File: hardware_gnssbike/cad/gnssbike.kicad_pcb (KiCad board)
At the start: 4 copper layers, 34 x 90 mm, 128 parts, among them J101 Molex 2036150003, J102 JST SM06B-GHS-TB, J103 contato de mola, 2 vias, J104 contato de mola, 2 vias, J105 contato de mola, 2 vias, J201 Tag-Connect TC2030-NL, J302 contato de mola, 2 vias, J401 Hirose FH28-10S-0.5SH, J402 Molex 503480-0500, Q401 DMG1012T-7, Q601 DMG1012T-7, Q602 DMG1012T-7, Q603 DMG1012T-7, SW601 Omron B3S-1002P, SW602 Omron B3S-1002P, SW603 Omron B3S-1002P, U101 nPM1300-QEAA, U102 MAX17262REWL, U103 AEM10900, U104 TPS7A0218PDQN, U201 MinewSemi ME54BS13, U301 u-blox MAX-F10S, U302 TI TXU0204BQAR, U501 MX25R6435F, U502 Bosch BMP585, U503 Bosch BMI270, U504 MMC5633NJL, U505 TI OPT3001DNPR

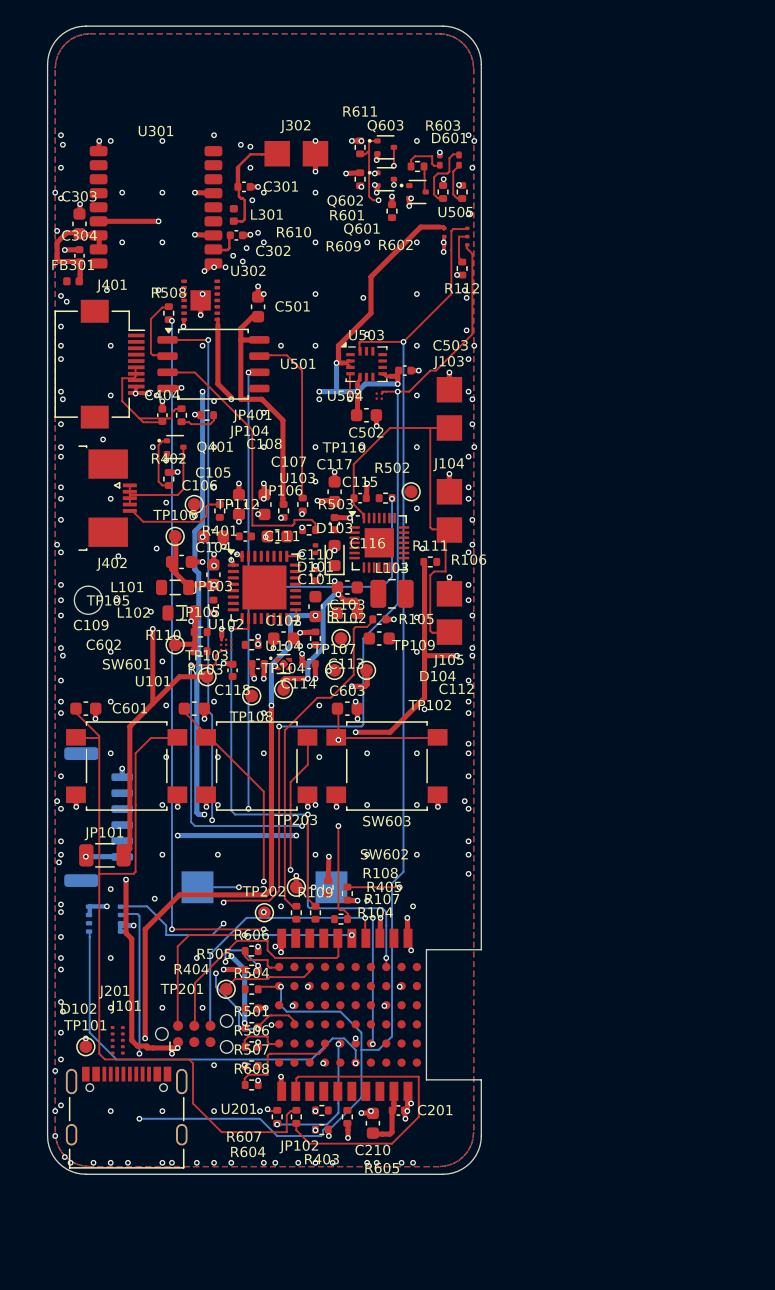
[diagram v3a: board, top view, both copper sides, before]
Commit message: feat(hardware): draw each part as its own symbol, not as a block
A rectangle with pin names down its sides is how an INTEGRATED CIRCUIT is
drawn, and only an integrated circuit. This generator drew all 127 parts
that way - resistors, ceramic capacitors, diodes, the TVS - and a sheet of
blocks joined by lines does not show a circuit.

Every class has its own symbol now, in the standard form, with the lead
axis on x and the body between -1.27 and +1.27 mm: a zigzag for a resistor
and a 0 ohm link (42 of them), two parallel plates for a ceramic capacitor
and a curved plate with a + for an electrolytic (31), four arcs for an
inductor (4), the same arcs inside a rectangle for a ferrite bead, which is
what tells the two apart, a zigzag with a diagonal arrow for the thermistor,
a triangle and a bar for a diode with arrows leaving it for an LED, two
contacts with a bar and a plunger for a key, a circle with a diagonal for
the buzzer, and a circle on the end of a lead for a test point. The 36 that
stay rectangles are the ones that should be: the ICs, the connectors and the
display. A two terminal part no longer prints pin numbers or pin names -
"1" and "2" on a resistor is noise, and the symbol already says which end is
which where it matters.

The power symbols had room reserved for the symbol and none for its NAME:
two ground pins two grid steps apart each got their own symbol, the symbols
did not collide, and the words printed over each other - "GNDGNDGND" along
the bottom of every chip. What is reserved now is the whole thing. With a
limit: the first cut let the stub run to fourteen grid steps looking for a
clear spot, and one of them crossed a component and split a net. A long stub
is worse than a crowded label, so it stops at eight and the label gives way.

One attempt is NOT in this commit, on purpose. Grouping every pin of a rail
on one edge into a single symbol - which is what a person draws - joins the
stubs with a line that runs along the part's edge and crosses w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
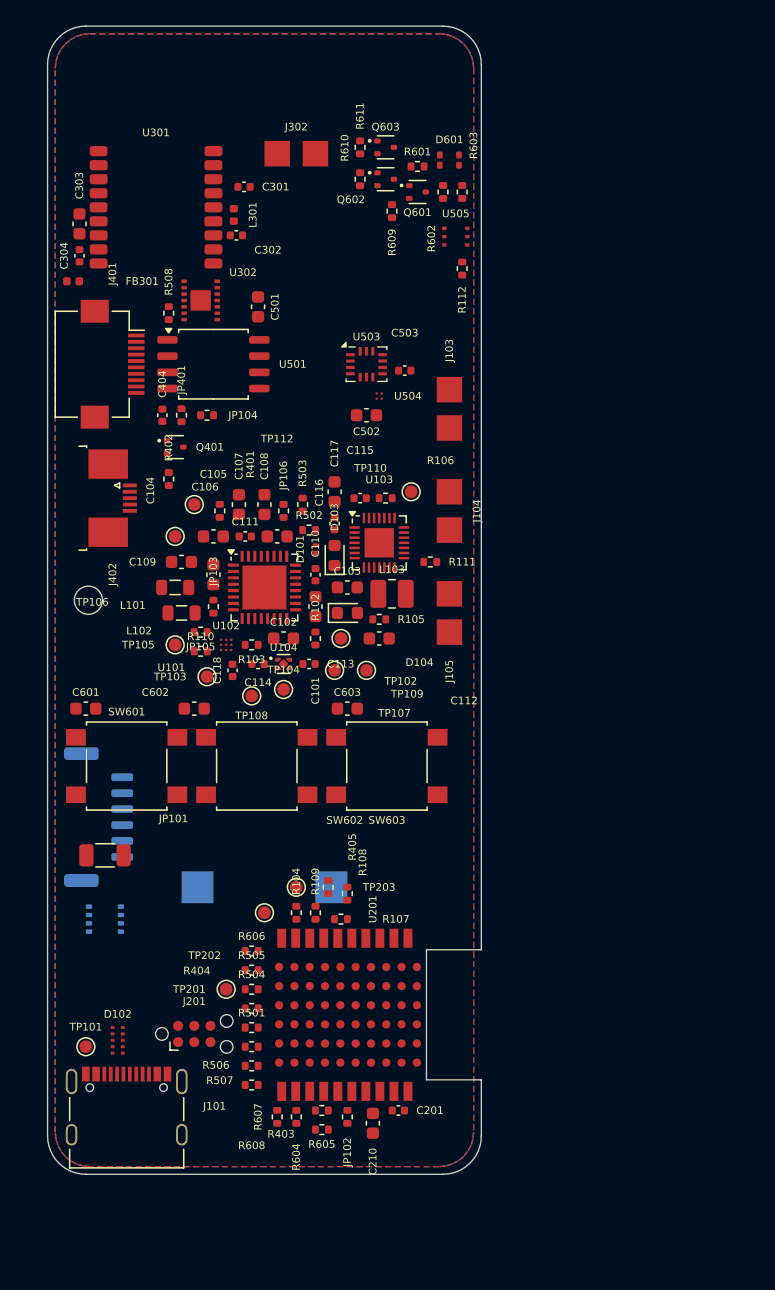
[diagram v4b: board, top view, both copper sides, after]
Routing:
- net 3V0: track 201.5 -> 0.00 mm, vias 18 -> 0
- net SENS_SDA: track 125.8 -> 0.00 mm, vias 4 -> 0
- net 3V0_SENS: track 108.0 -> 0.00 mm, vias 9 -> 0
- net SENS_SCL: track 86.6 -> 0.00 mm, vias 6 -> 0
- net RGB_B: track 74.7 -> 0.00 mm, vias 2 -> 0
- net KEY_L_SW: track 66.9 -> 0.00 mm
- net VBCKP: track 65.4 -> 0.00 mm, vias 3 -> 0
- net NOR_CS: track 63.5 -> 0.00 mm, vias 4 -> 0
- net NOR_MISO: track 63.1 -> 0.00 mm, vias 4 -> 0
- net GND: track 62.1 -> 0.00 mm, vias 285 -> 0
- net VSYS: track 55.8 -> 0.00 mm, vias 5 -> 0
- net KEY_C_SW: track 54.7 -> 0.00 mm, vias 3 -> 0
- net NOR_SCK_F: track 54.0 -> 0.00 mm, vias 3 -> 0
- net IMU_INT: track 53.4 -> 0.00 mm, vias 3 -> 0
- net SD3V0: track 53.4 -> 0.00 mm, vias 6 -> 0
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
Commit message: feat(hardware): a u.FL for the GNSS antenna, and an assembly drawing that reads
The GNSS antenna arrived on a spring contact. The line it feeds is the
L1 + L5 path of the MAX-F10S and section 4.4 of the integration manual asks
for 50 ohm on ALL of it - and a pair of gold pads that a leaf spring presses
on has no defined impedance at 1.2 and 1.6 GHz, no defined return path, and
a contact resistance that changes with how the case was closed. J302 is a
Hirose U.FL-R-SMT-1 now, the 50 ohm coaxial transition every GNSS module
reference design uses for an external element. It costs 2.6 x 2.6 mm of
board and trades a mechanical fit for a cable, which is a mechanical
decision that was recorded nowhere. The RF path went from 8.2 to 5.7 mm.
The three solar spring contacts stay spring contacts: no RF there.

And the assembly drawing stopped coming out of a KiCad layer, because
neither layer can give one for this board. Silkscreen is silkscreen: it
obeys manufacturing, 0.6 mm of text, and 127 designators on a 34 x 90 mm
board at 48% occupancy do not fit around the parts without landing on one
another or drifting so far from the part that they name nothing. F.Fab
carries whatever each library footprint put there, at whatever size its
author chose, plus the value - "TP110" at 1.0 mm beside "100 nF" at 0.5,
both over the outline.

An assembly drawing is not a copper layer. It is a drawing, and it may do
the one thing a silkscreen may not: put the label where it can be read and
draw a LINE from the label to the part. montagem.py does that - the
reference inside the courtyard where it fits, outside with a dot and a
leader where it does not. 92 of the 127 need the leader.

The silkscreen placement was also backwards: it preferred a spot clear of
ANY part's outline to a spot near its own, which on a board this dense
pushes the designator millimetres away and produces a cloud where nothing
points at anything. Proximity decides now - nearest first, the first
candidate that misses every 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
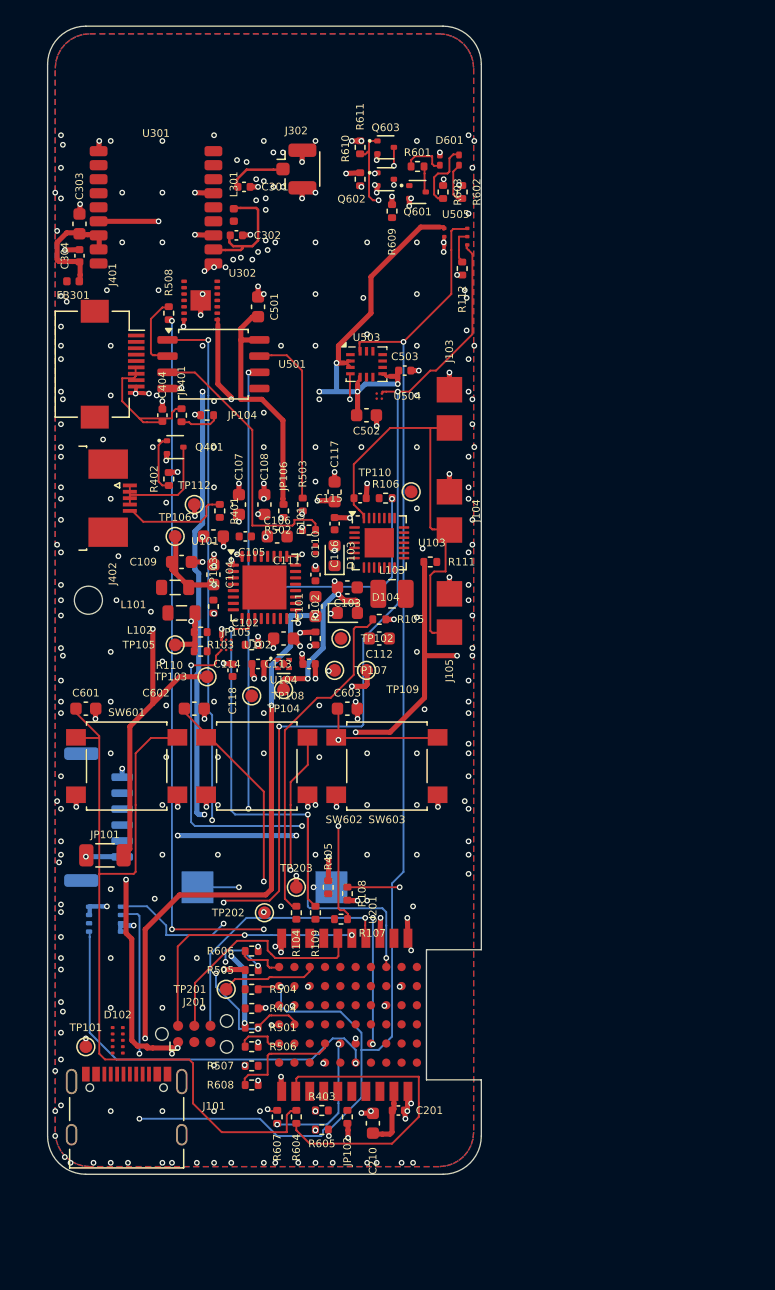
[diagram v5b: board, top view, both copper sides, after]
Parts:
- J302: value contato de mola, 2 vias -> Hirose U.FL-R-SMT-1; footprint gnssbike:ContatoMola_2x2mm_P3mm -> Connector_Coaxial:U.FL_Hirose_U.FL-R-SMT-1_Vertical
- moved J302 1.20 mm to (44.5, 36.2)
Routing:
- net 3V0: track 0.00 -> 201.5 mm, vias 0 -> 18
- net SENS_SDA: track 0.00 -> 125.8 mm, vias 0 -> 4
- net 3V0_SENS: track 0.00 -> 108.0 mm, vias 0 -> 9
- net SENS_SCL: track 0.00 -> 86.6 mm, vias 0 -> 6
- net RGB_B: track 0.00 -> 74.7 mm, vias 0 -> 2
- net KEY_L_SW: track 0.00 -> 66.9 mm
- net VBCKP: track 0.00 -> 65.4 mm, vias 0 -> 3
- net NOR_CS: track 0.00 -> 63.5 mm, vias 0 -> 4
- net NOR_MISO: track 0.00 -> 63.1 mm, vias 0 -> 4
- net GND: track 0.00 -> 62.5 mm, vias 0 -> 295
- net VSYS: track 0.00 -> 55.8 mm, vias 0 -> 5
- net KEY_C_SW: track 0.00 -> 54.7 mm, vias 0 -> 3
- net NOR_SCK_F: track 0.00 -> 54.0 mm, vias 0 -> 3
- net IMU_INT: track 0.00 -> 53.4 mm, vias 0 -> 3
- net SD3V0: track 0.00 -> 53.4 mm, vias 0 -> 6
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
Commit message: feat(hardware): buy what JLCPCB can actually assemble
The board is made and assembled at JLCPCB, so every part has to be one
LCSC stocks - the owner's rule of 2026-09-24, with the Minew module and
the solar cells as the only exceptions. Three surveys against LCSC's
catalogue and JLCPCB's assembly API checked the 34 parts that are not a
plain resistor or capacitor, and this is what came back.

Parts that changed, and what each change costs:

  J101  Molex 2036150003 -> HRO TYPE-C-31-M-12 (C165948). 309 in the
        world at US$ 5,69 against 91.943 at US$ 0,186, and KiCad carries
        the land pattern under the part's own name. The body goes from
        8,58 to 7,35 mm, so the case opening changes.
  D101  ESD761DPYR -> TPD1E05U06DPYR (C436349). Same X1SON-2 and better
        capacitance, but bidirectional 24 V becomes unidirectional
        5,5 V: orientation now matters and a faulty cable putting 20 V
        on a CC line is no longer survivable.
  J103  three pairs of spring pads -> one JST ZH of 4 ways, with three
        0 ohm joining the groups to SRC. Nobody assembles a spring, a
        bicycle vibrates, and a pressed contact that opens and closes on
        the input of a switching converter is a dirty transient. ZH of
        1,5 mm on purpose: the cell is a GH of 1,25 and 4,2 V into the
        harvester's 2,73 V input would kill it. The 0 ohm let one face
        be measured alone in the sun.
  D105  new: a clamp on SRC. The right connector stops the mistake; the
        clamp stops the damage when the mistake comes from a crimp.
  J101  the shell had no pin, so four pads of the land pattern floated.

U101 and U103 stay as they are and go by consignment: the nPM1300 QFN is
zero on both sides and the whole e-peas line is zero. The nPM1300 does
exist in WLCSP-35, but its 0,419 x 0,440 mm ball pitch is smaller than
this board's 0,45 mm via and would force via-in-pad on every board ever
made, probably six layers, twice the thermal resistance and a light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
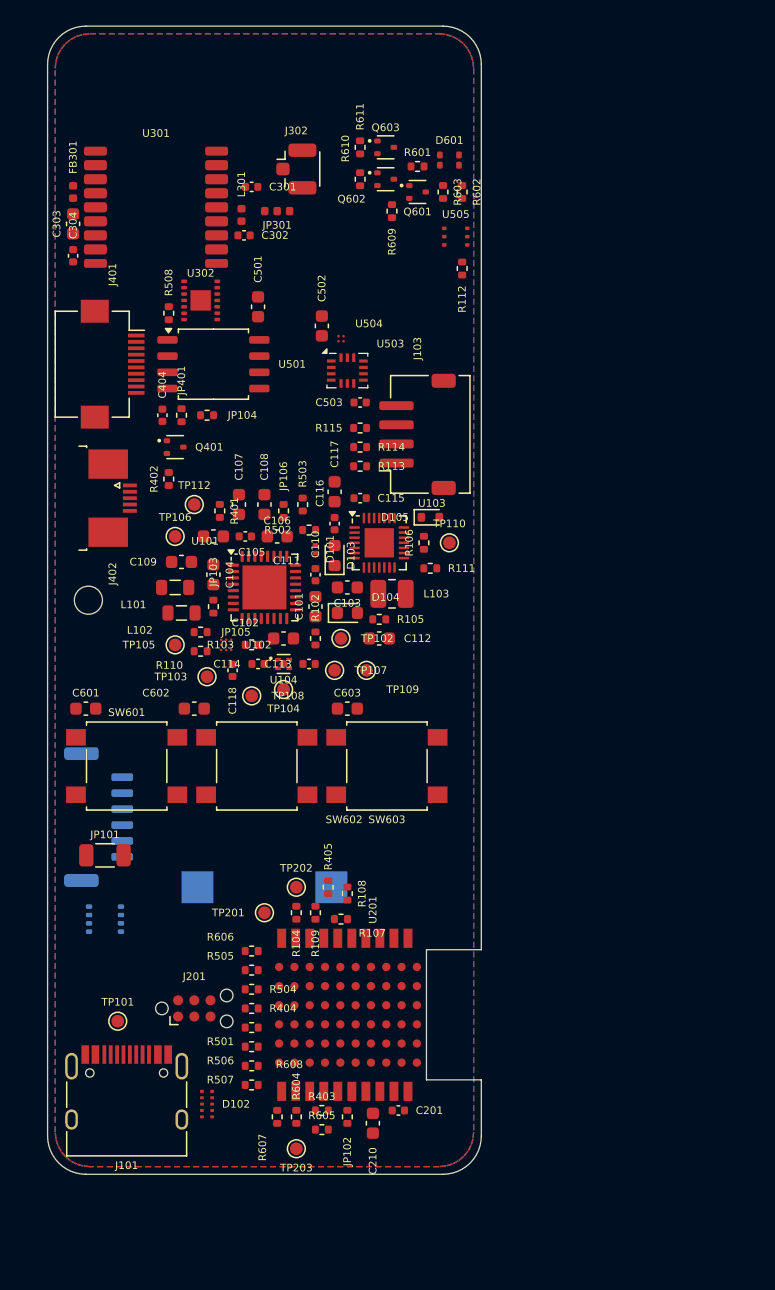
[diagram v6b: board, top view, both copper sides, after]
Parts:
- removed J104, J105: contato de mola, 2 vias, gnssbike:ContatoMola_2x2mm_P3mm
- added D105: TVS 3,0 V, Diode_SMD:D_SOD-523, F.Cu at (55.0, 63.5)
- added JP301: 0 R, gnssbike:JumperRF_3x0402, F.Cu at (43.0, 39.5)
- added R113: 0 R, Resistor_SMD:R_0402_1005Metric, F.Cu at (49.5, 59.5)
- added R114: 0 R, Resistor_SMD:R_0402_1005Metric, F.Cu at (49.5, 58.0)
- added R115: 0 R, Resistor_SMD:R_0402_1005Metric, F.Cu at (49.5, 56.5)
- D101: value ESD761DPYR -> TPD1E05U06DPYR
- J101: value Molex 2036150003 -> HRO TYPE-C-31-M-12; footprint Connector_USB:USB_C_Receptacle_Palconn_UTC16-G -> Connector_USB:USB_C_Receptacle_HRO_TYPE-C-31-M-12
- J103: value contato de mola, 2 vias -> JST S4B-ZR-SM4A-TF; footprint gnssbike:ContatoMola_2x2mm_P3mm -> Connector_JST:JST_ZH_S4B-ZR-SM4A-TF_1x04-1MP_P1.50mm_Horizontal
- U301: footprint gnssbike:u-blox_MAX-F10S_9.7x10.1mm -> gnssbike:u-blox_MAX_LCC-18_9.7x10.1mm
- U501: footprint Package_SO:SOIC-8_5.23x5.23mm_P1.27mm -> Package_SO:SOIC-8_5.275x5.275mm_P1.27mm
- moved TP203 20.5 mm to (44.5, 113.0)
- moved D102 8.60 mm to (37.5, 109.5)
- moved C502 7.83 mm to (46.5, 48.5), turned to 90 degrees
- moved FB301 7.00 mm to (27.0, 38.0), turned to 90 degrees
- moved TP201 6.71 mm to (42.0, 94.5)
- moved U504 5.41 mm to (48.0, 49.5)
- moved TP110 5.00 mm to (56.5, 65.5)
- moved R106 4.61 mm to (54.5, 65.5), turned to 90 degrees
- moved C503 4.30 mm to (49.5, 54.5)
- moved J103 3.20 mm to (54.0, 57.0)
- moved TP101 3.20 mm to (30.5, 103.0)
- moved TP202 3.20 mm to (44.5, 92.5)
- moved J201 2.00 mm to (36.5, 102.0)
- moved U503 1.58 mm to (48.5, 52.0)
- moved C301 0.60 mm to (41.0, 37.6)
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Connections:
- J101 pad S1: (no net) -> GND
- J103 pad 1: SRC -> PV_A
- J103 pad 2: GND -> PV_B
- J302 pad 1: RF_ANT -> RF_UFL
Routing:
- net 3V0: track 201.5 -> 0.00 mm, vias 18 -> 0
- net SENS_SDA: track 125.8 -> 0.00 mm, vias 4 -> 0
- net 3V0_SENS: track 108.0 -> 0.00 mm, vias 9 -> 0
- net SENS_SCL: track 86.6 -> 0.00 mm, vias 6 -> 0
- net RGB_B: track 74.7 -> 0.00 mm, vias 2 -> 0
- net KEY_L_SW: track 66.9 -> 0.00 mm
- net VBCKP: track 65.4 -> 0.00 mm, vias 3 -> 0
- net NOR_CS: track 63.5 -> 0.00 mm, vias 4 -> 0
- net NOR_MISO: track 63.1 -> 0.00 mm, vias 4 -> 0
- net GND: track 62.5 -> 0.00 mm, vias 295 -> 0
- net VSYS: track 55.8 -> 0.00 mm, vias 5 -> 0
- net KEY_C_SW: track 54.7 -> 0.00 mm, vias 3 -> 0
- net NOR_SCK_F: track 54.0 -> 0.00 mm, vias 3 -> 0
- net IMU_INT: track 53.4 -> 0.00 mm, vias 3 -> 0
- net SD3V0: track 53.4 -> 0.00 mm, vias 6 -> 0
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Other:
- board text added: "130 pecas colocadas, 8 fora da placa (painel, antena e modulos solares vivem na caixa)"
- board text removed: "127 pecas colocadas, 8 fora da placa (painel, antena e modulos solares vivem na caixa)"
